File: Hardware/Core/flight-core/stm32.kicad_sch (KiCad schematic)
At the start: 27 parts, among them J1 Conn_01x04_Socket, SW1 SW_SPDT, SW2 SW_MEC_5G, U1 STM32G473CCTx, U13 MCP23S17_SS, U402 TCAN1042VDRQ1, Y1 48 MHZ

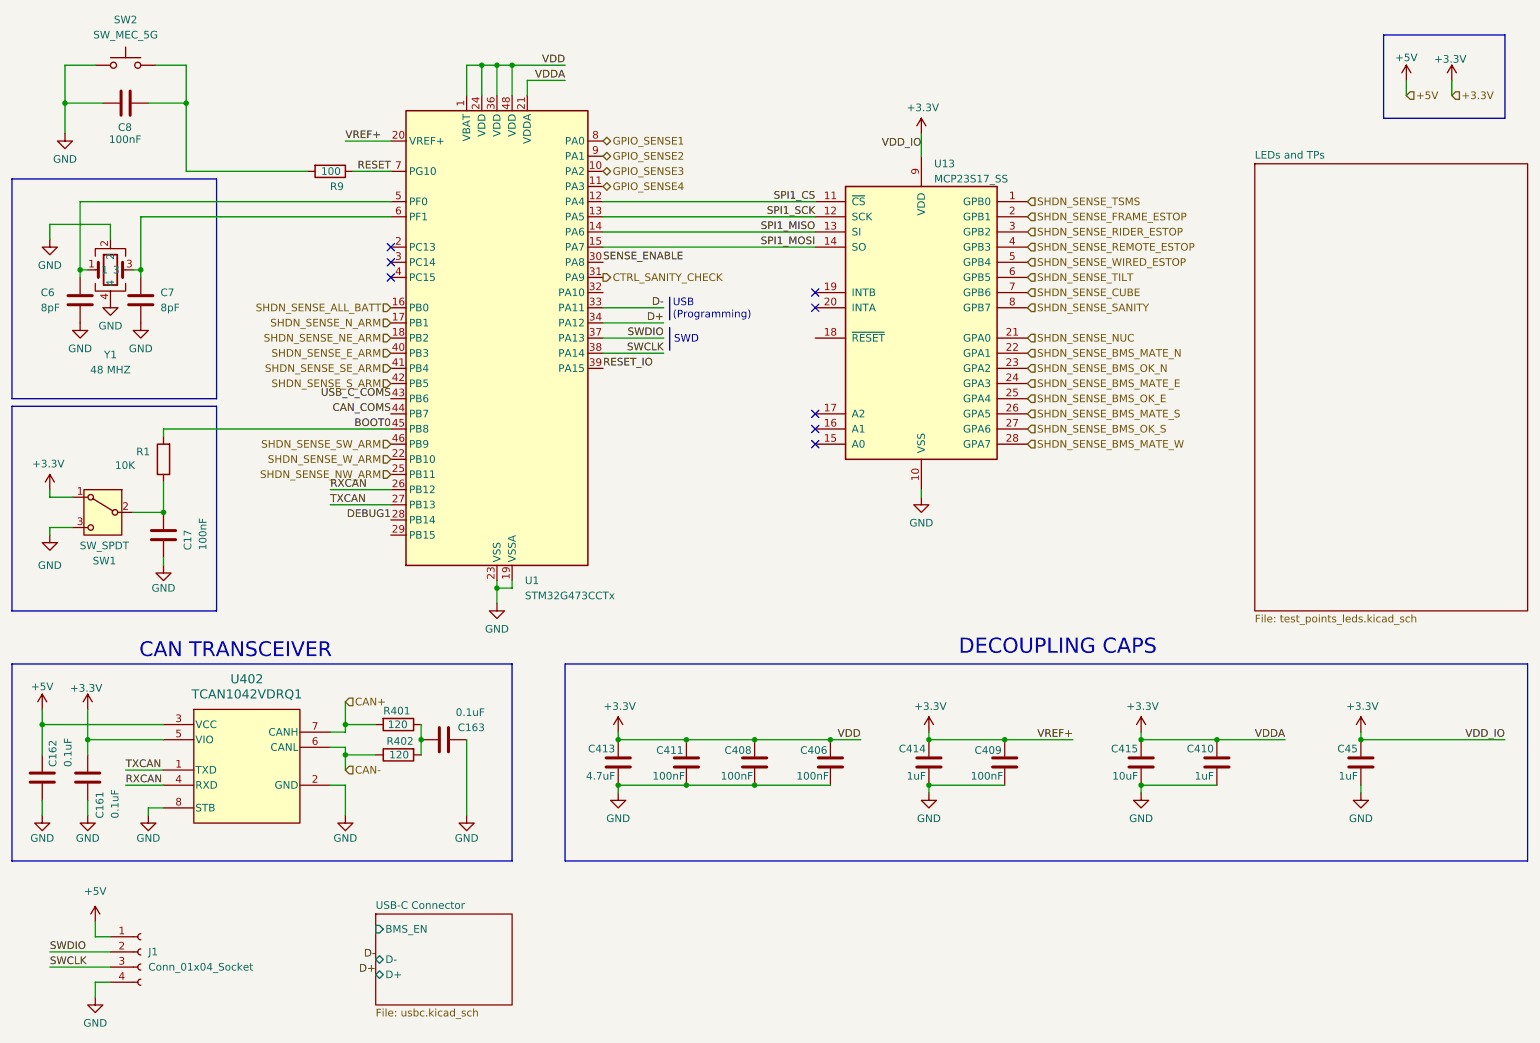
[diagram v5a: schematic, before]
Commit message: added 5V to USBC VBUS to power by usb; edited stm32 file to match
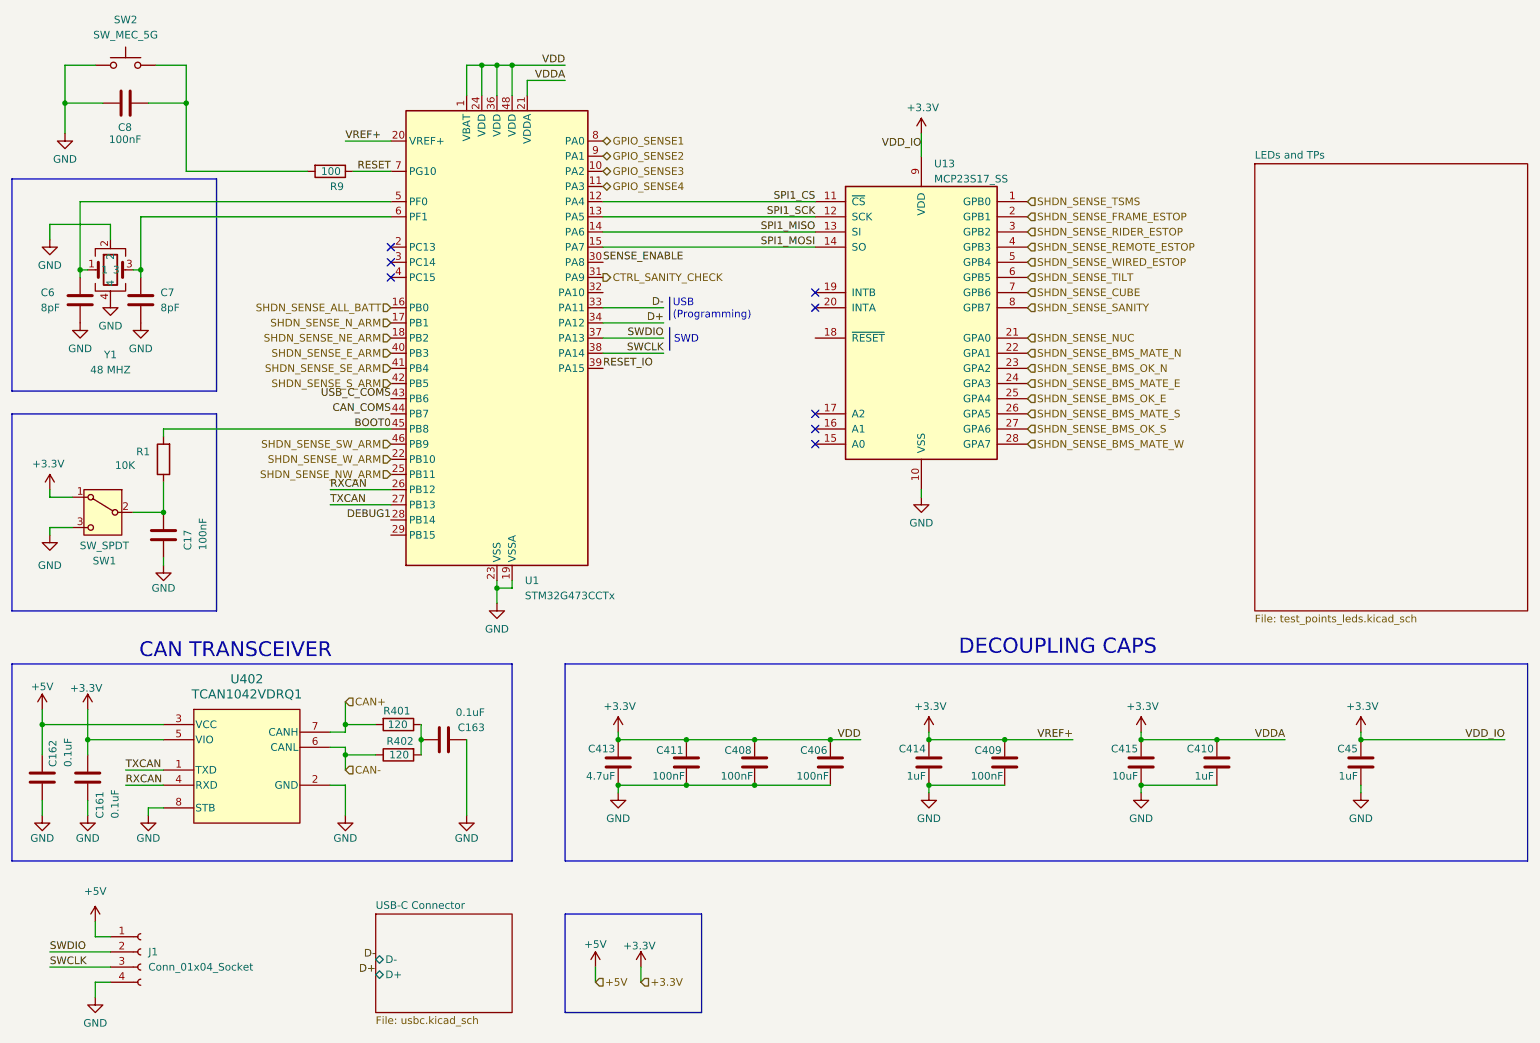
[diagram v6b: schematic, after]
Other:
- sheet USB-C Connector ports: added none; removed BMS_EN
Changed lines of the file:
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@@
 	)
 	(rectangle
-		(start 255.27 24.13)
-		(end 275.59 38.1)
+		(start 118.11 171.45)
+		(end 140.97 187.96)
 		(stroke
 			(width 0)
@@
 	(rectangle
 		(start 25.4 48.26)
-		(end 59.69 85.09)
+		(end 59.69 83.82)
 		(stroke
 			(width 0)
@@
 	)
 	(rectangle
-		(start 25.4 86.36)
+		(start 25.4 87.63)
 		(end 59.69 120.65)
 		(stroke
@@
 	(wire
 		(pts
-			(xy 259.08 31.75) (xy 259.08 34.29)
+			(xy 123.19 180.34) (xy 123.19 182.88)
 		)
 		(stroke
@@
 	(wire
 		(pts
-			(xy 266.7 31.75) (xy 266.7 34.29)
+			(xy 130.81 180.34) (xy 130.81 182.88)
 		)
 		(stroke
@@
 	(hierarchical_label "+3.3V"
 		(shape input)
-		(at 266.7 34.29 0)
+		(at 130.81 182.88 0)
 		(effects
 			(font
@@
 	(hierarchical_label "+5V"
 		(shape input)
-		(at 259.08 34.29 0)
+		(at 123.19 182.88 0)
 		(effects
 			(font
@@
 	(symbol
 		(lib_id "power:+3.3V")
-		(at 266.7 31.75 0)
+		(at 130.81 180.34 0)
 		(unit 1)
 		(exclude_from_sim no)
@@
 		(dnp no)
 		(property "Reference" "#PWR0429"
-			(at 266.7 35.56 0)
+			(at 130.81 184.15 0)
 			(effects
 				(font
@@
 		)
 		(property "Value" "+3.3V"
-			(at 266.446 28.194 0)
+			(at 130.556 176.784 0)
 			(effects
 				(font
@@
 		)
 		(property "Footprint" ""
-			(at 266.7 31.75 0)
+			(at 130.81 180.34 0)
 			(effects
 				(font
@@
 		)
 		(property "Datasheet" ""
-			(at 266.7 31.75 0)
+			(at 130.81 180.34 0)
 			(effects
 				(font
@@
 		)
 		(property "Description" "Power symbol creates a global label with name \"+3.3V\""
-			(at 266.7 31.75 0)
+			(at 130.81 180.34 0)
 			(effects
 				(font
@@
 	(symbol
 		(lib_id "power:+5V")
-		(at 259.08 31.75 0)
+		(at 123.19 180.34 0)
 		(unit 1)
 		(exclude_from_sim no)
@@
 		(dnp no)
 		(property "Reference" "#PWR0428"
-			(at 259.08 35.56 0)
+			(at 123.19 184.15 0)
 			(effects
 				(font
@@
 		)
 		(property "Value" "+5V"
-			(at 259.08 27.94 0)
+			(at 123.19 176.53 0)
 			(effects
 				(font
@@
 		)
 		(property "Footprint" ""
-			(at 259.08 31.75 0)
+			(at 123.19 180.34 0)
 			(effects
 				(font
@@
 		)
 		(property "Datasheet" ""
-			(at 259.08 31.75 0)
+			(at 123.19 180.34 0)
 			(effects
 				(font
@@
 		)
 		(property "Description" ""
-			(at 259.08 31.75 0)
+			(at 123.19 180.34 0)
 			(effects
 				(font
@@
 	(sheet
 		(at 86.36 171.45)
-		(size 22.86 15.24)
+		(size 22.86 16.51)
 		(exclude_from_sim no)
 		(in_bom yes)
@@
 		)
 		(property "Sheetfile" "usbc.kicad_sch"
-			(at 86.36 187.2746 0)
+			(at 86.36 188.5446 0)
 			(effects
 				(font
@@
 			)
 		)
-		(pin "BMS_EN" input
-			(at 86.36 173.99 180)
-			(effects
-				(font
-					(size 1.27 1.27)
-				)
-				(justify left)
-			)
-		)

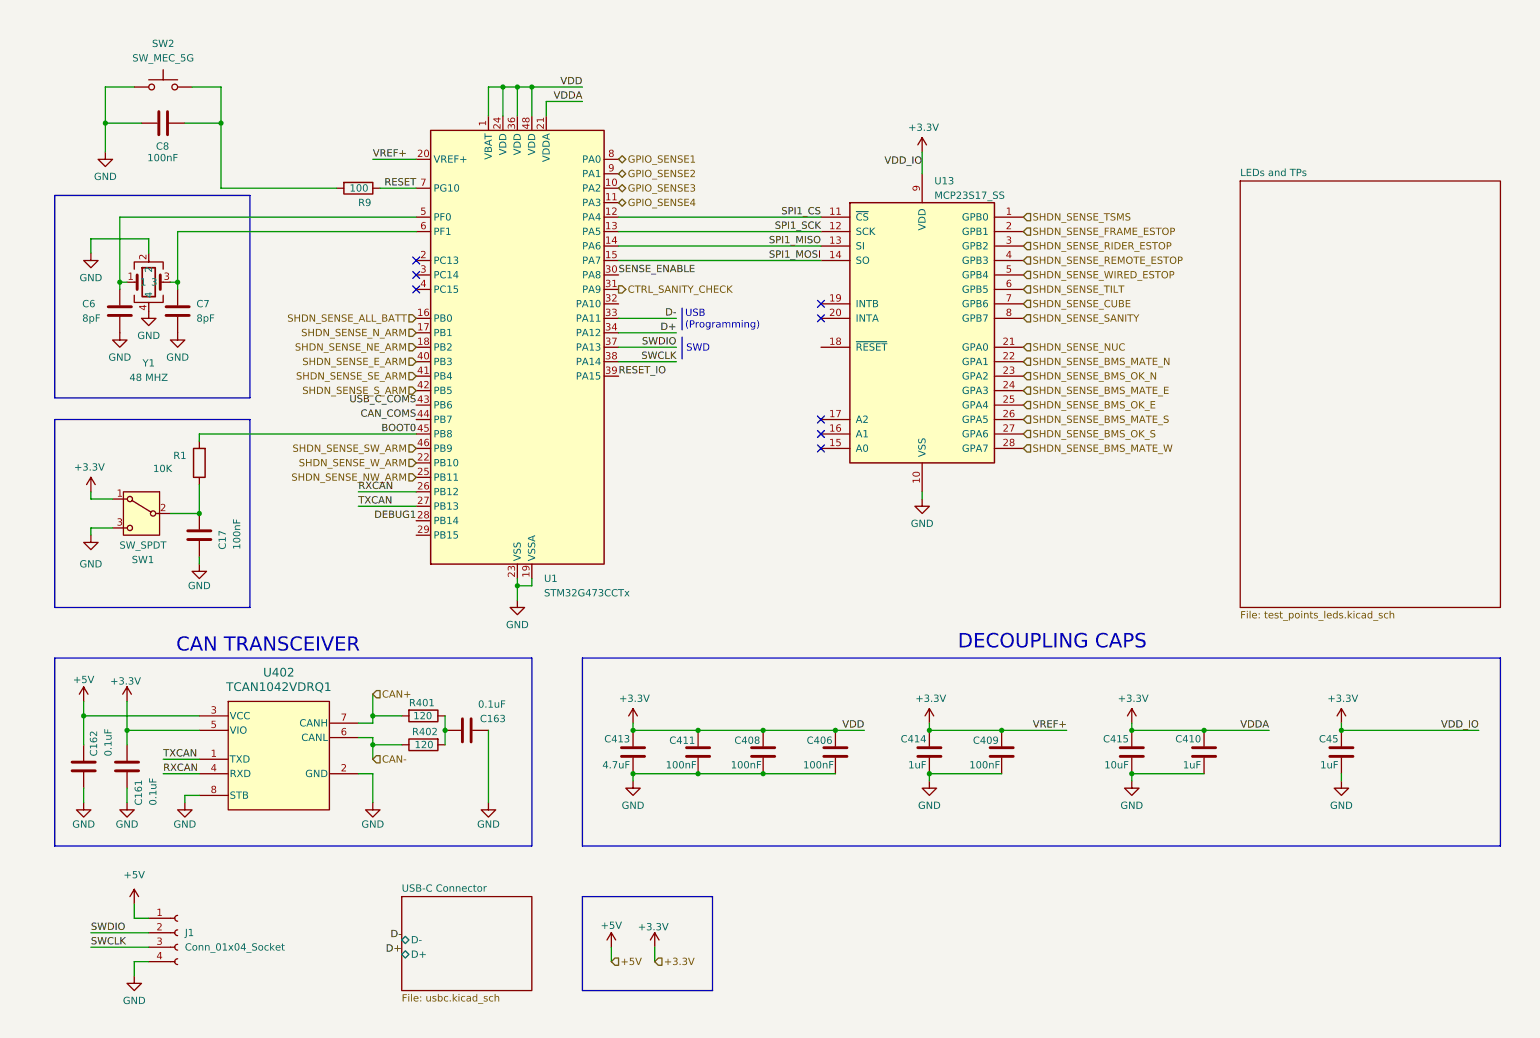
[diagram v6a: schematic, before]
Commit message: updated boot0 & hierarchical LED sheet, connected all io, added display & reorganized
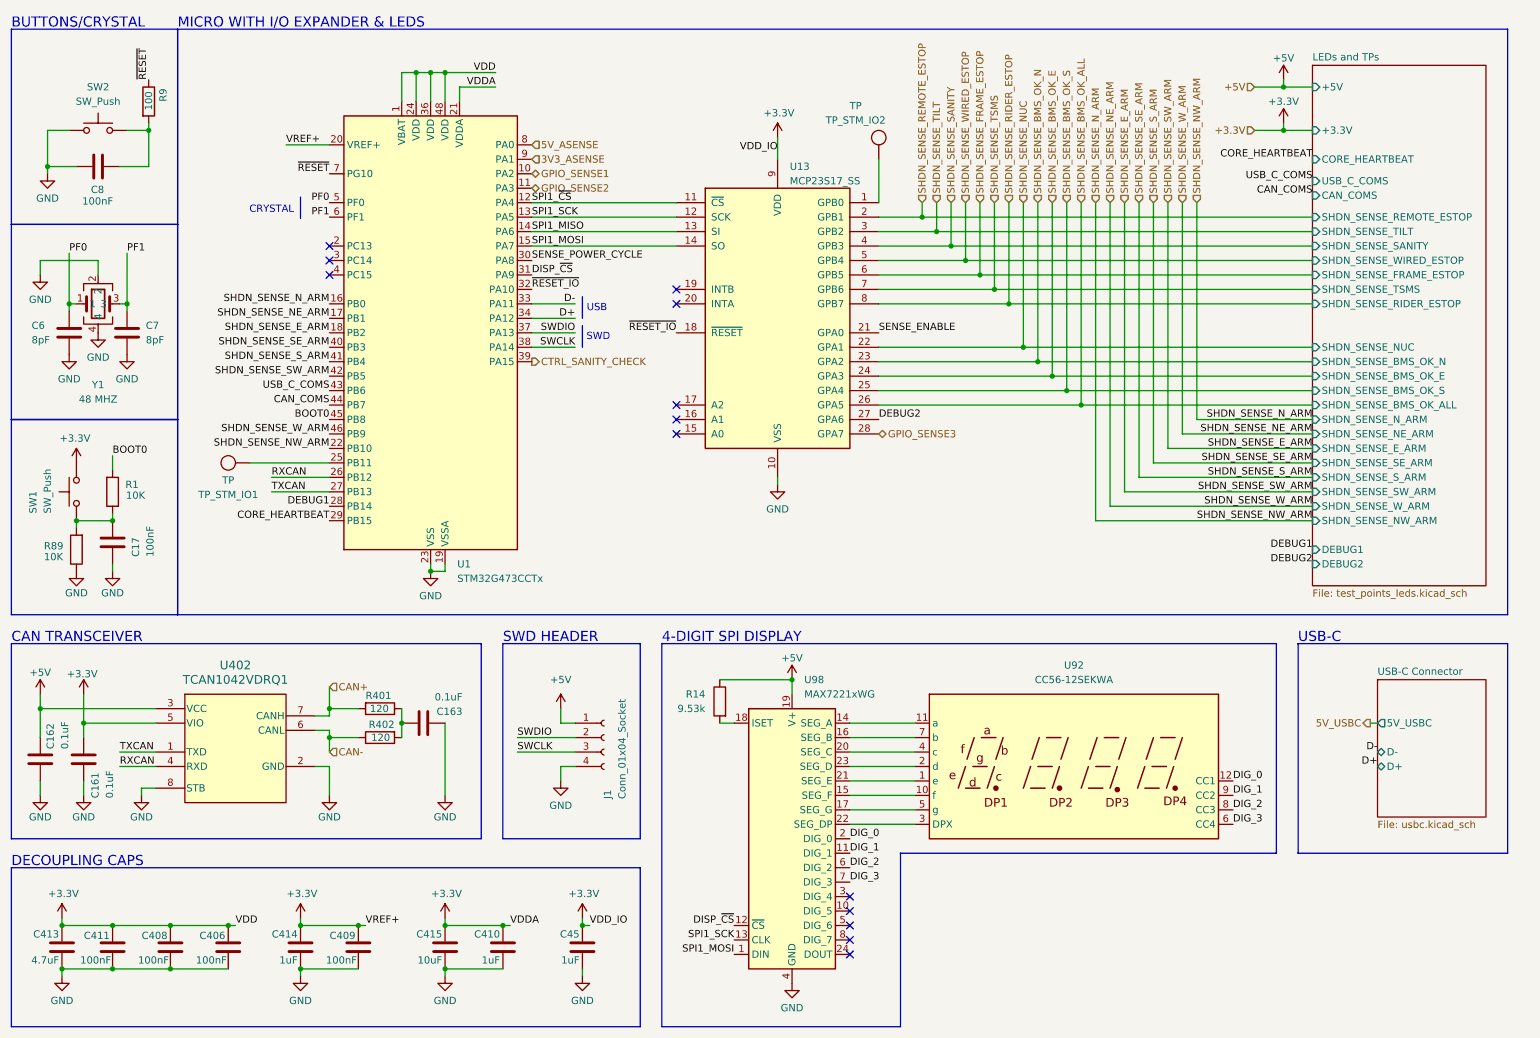
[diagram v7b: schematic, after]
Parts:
- removed SW1: SW_SPDT, symbol Switch:SW_SPDT
- removed SW2: SW_MEC_5G, Button_Switch_SMD:SW_MEC_5GSH9, symbol Switch:SW_MEC_5G
- added R14: 9.53k, footprints:R_0603_1608Metric, symbol Device:R
- added R89: 10K, footprints:R_0805_OEM, symbol formula:R_10K
- added SW1, SW2: SW_Push, symbol Switch:SW_Push
- added TP_STM_IO1, TP_STM_IO2: TP, footprints:tp_1.6mm, symbol formula:TP
- added U92: CC56-12SEKWA, Display_7Segment:CA56-12SEKWA, symbol Display_Character:CC56-12SEKWA
- added U98: MAX7221xWG, Package_SO:SOIC-24W_7.5x15.4mm_P1.27mm, symbol Driver_LED:MAX7221xWG
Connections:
- net GPIO_SENSE4 is gone; now on net GPIO_SENSE2: U1.11 (PA3)
- net RESET_IO is gone; now on net CTRL_SANITY_CHECK: U1.39 (PA15)
- net SHDN_SENSE_ALL_BATT is gone; now on net SHDN_SENSE_NW_ARM: U1.16 (PB0)
- net SHDN_SENSE_BMS_MATE_E is gone; now on net SHDN_SENSE_BMS_OK_E: U13.24 (GPA3)
- net SHDN_SENSE_BMS_MATE_N is gone; now on net SHDN_SENSE_NUC: U13.22 (GPA1)
- net SHDN_SENSE_BMS_MATE_W is gone; now on net GPIO_SENSE3: U13.28 (GPA7)
- net SHDN_SENSE_CUBE is gone; now on net SHDN_SENSE_TSMS: U13.7 (GPB6)
- net SHDN_SENSE_N_ARM is gone; now on net SHDN_SENSE_NE_ARM: U1.17 (PB1)
- net SHDN_SENSE_SW_ARM is gone; now on net SHDN_SENSE_NE_ARM: U1.46 (PB9)
- net SHDN_SENSE_S_ARM is gone; now on net SHDN_SENSE_E_ARM: U1.42 (PB5)
- net SHDN_SENSE_W_ARM is gone; now on net SHDN_SENSE_NW_ARM: U1.22 (PB10)
- net +3.3V: now also SW1.1
- net +5V: now also R14.1, U98.19 (V+)
- net CTRL_SANITY_CHECK: no longer U1.31 (PA9)
- net GND: now also R89.1, SW2.1, U98.4 (GND), U98.9 (GND)
- net GPIO_SENSE1: now also U1.10 (PA2); no longer U1.8 (PA0)
- net GPIO_SENSE2: no longer U1.9 (PA1)
- net GPIO_SENSE3: no longer U1.10 (PA2)
- net SENSE_ENABLE: now also U13.21 (GPA0); no longer U1.30 (PA8)
- net SHDN_SENSE_BMS_OK_E: no longer U13.25 (GPA4)
- net SHDN_SENSE_BMS_OK_S: now also U13.25 (GPA4); no longer U13.27 (GPA6)
- net SHDN_SENSE_E_ARM: now also U1.18 (PB2); no longer U1.40 (PB3)
- net SHDN_SENSE_FRAME_ESTOP: now also U13.6 (GPB5); no longer U13.2 (GPB1)
- net SHDN_SENSE_NE_ARM: no longer U1.18 (PB2)
- net SHDN_SENSE_NUC: no longer U13.21 (GPA0)
- net SHDN_SENSE_NW_ARM: no longer U1.25 (PB11)
- net SHDN_SENSE_REMOTE_ESTOP: now also U13.2 (GPB1); no longer U13.4 (GPB3)
- net SHDN_SENSE_RIDER_ESTOP: now also U13.8 (GPB7); no longer U13.3 (GPB2)
- net SHDN_SENSE_SANITY: now also U13.4 (GPB3); no longer U13.8 (GPB7)
- net SHDN_SENSE_SE_ARM: now also U1.40 (PB3)
- net SHDN_SENSE_TILT: now also U13.3 (GPB2); no longer U13.6 (GPB5)
- net SHDN_SENSE_TSMS: no longer U13.1 (GPB0)
- net SPI1_MOSI: now also U98.1 (DIN)
- net SPI1_SCK: now also U98.13 (CLK)
- net PF0: now reaches C6.1, U1.5 (PF0), Y1.1
- net PF1: now reaches C7.1, U1.6 (PF1), Y1.3
- net ~{RESET_IO}: now reaches U13.18 (~{RESET})
- net ~{RESET_IO}: now also U1.32 (PA10)
- net CORE_HEARTBEAT: now reaches U1.29 (PB15)
- net at C8.2, R9.2: now also SW2.2
- net at C17.1, R1.1: now also R89.2, SW1.2
- net RESET renamed ~{RESET}
- net SHDN_SENSE_BMS_MATE_S renamed SHDN_SENSE_BMS_OK_ALL
- net SPI1_CS renamed SPI1_~{CS}
- new net: TP_STM_IO2.1 (TP), U13.1 (GPB0)
- new net: U92.11 (a), U98.14 (SEG_A)
- new net: U92.10 (f), U98.15 (SEG_F)
- new net: U92.7 (b), U98.16 (SEG_B)
- new net: U92.5 (g), U98.17 (SEG_G)
- new net: R14.2, U98.18 (ISET)
- new net: U92.4 (c), U98.20 (SEG_C)
- new net: U92.1 (e), U98.21 (SEG_E)
- new net: U92.3 (DPX), U98.22 (SEG_DP)
- new net: U92.2 (d), U98.23 (SEG_D)
- new net: TP_STM_IO1.1 (TP), U1.25 (PB11)
- new net 3V3_ASENSE: U1.9 (PA1)
- new net 5V_ASENSE: U1.8 (PA0)
- new net DEBUG2: U13.27 (GPA6)
- new net DIG_0: U92.12 (CC1), U98.2 (DIG_0)
- new net DIG_1: U92.9 (CC2), U98.11 (DIG_1)
- new net DIG_2: U92.8 (CC3), U98.6 (DIG_2)
- new net DIG_3: U92.6 (CC4), U98.7 (DIG_3)
- new net DISP_~{CS}: U1.31 (PA9), U98.12 (~{CS})
- new net SENSE_POWER_CYCLE: U1.30 (PA8)
- no-connect marks 8 -> 13
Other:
- sheet LEDs and TPs ports: added +3.3V, +5V, CAN_COMS, CORE_HEARTBEAT, DEBUG1, DEBUG2, SHDN_SENSE_BMS_OK_ALL, SHDN_SENSE_BMS_OK_E, SHDN_SENSE_BMS_OK_N, SHDN_SENSE_BMS_OK_S, SHDN_SENSE_E_ARM, SHDN_SENSE_FRAME_ESTOP, SHDN_SENSE_NE_ARM, SHDN_SENSE_NUC, SHDN_SENSE_NW_ARM, SHDN_SENSE_N_ARM, SHDN_SENSE_REMOTE_ESTOP, SHDN_SENSE_RIDER_ESTOP, SHDN_SENSE_SANITY, SHDN_SENSE_SE_ARM, SHDN_SENSE_SW_ARM, SHDN_SENSE_S_ARM, SHDN_SENSE_TILT, SHDN_SENSE_TSMS, SHDN_SENSE_WIRED_ESTOP, SHDN_SENSE_W_ARM, USB_C_COMS; removed none
- sheet USB-C Connector ports: added 5V_USBC; removed none
- note added: "4-DIGIT SPI DISPLAY"
- note added: "BUTTONS/CRYSTAL"
- note added: "CRYSTAL"
- note added: "MICRO WITH I/O EXPANDER & LEDS"
- note added: "SWD HEADER"
- note added: "USB"
- note added: "USB-C"
- note removed: "USB (Programming)"
- moved on the sheet: C161, C162, C163, C17, C406, C408, C409, C410, C411, C413, C414, C415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

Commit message: top sheet reorg
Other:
- moved on the sheet: C6, C7, C8, R9, SW2, Y1
